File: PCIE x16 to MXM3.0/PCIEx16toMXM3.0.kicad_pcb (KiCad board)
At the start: 4 copper layers, 167.6 x 106.5 mm, 16 parts, among them J1 Bus_PCI_Express_x16, J2 MXM3.0, J4 2040210-1_NonStock, J5 74320-9010, U1 AMS1117-5.0

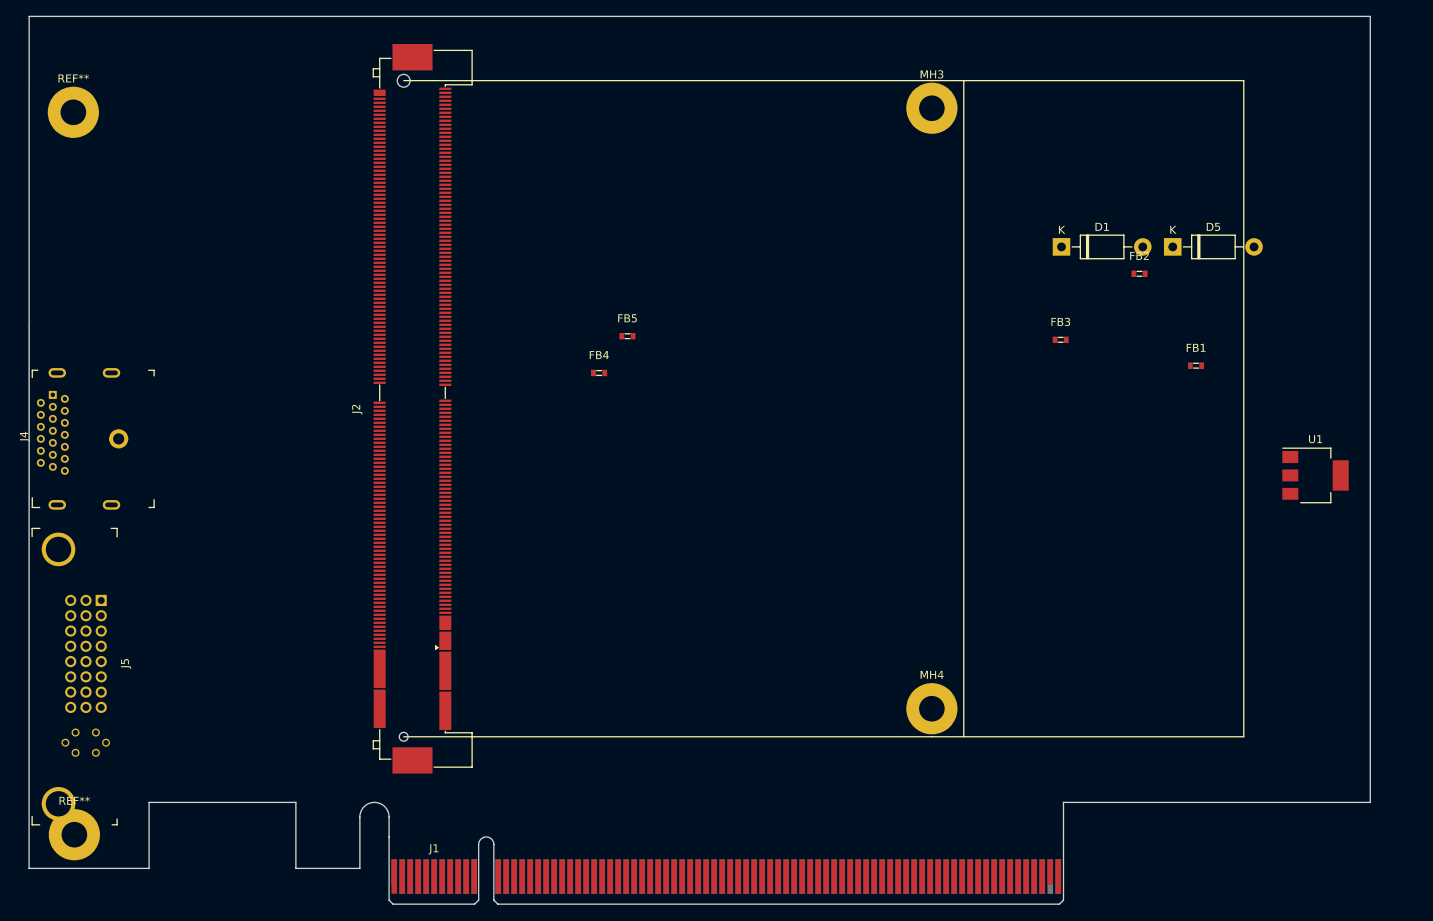
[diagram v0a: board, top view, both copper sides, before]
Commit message: Added x16 prototype
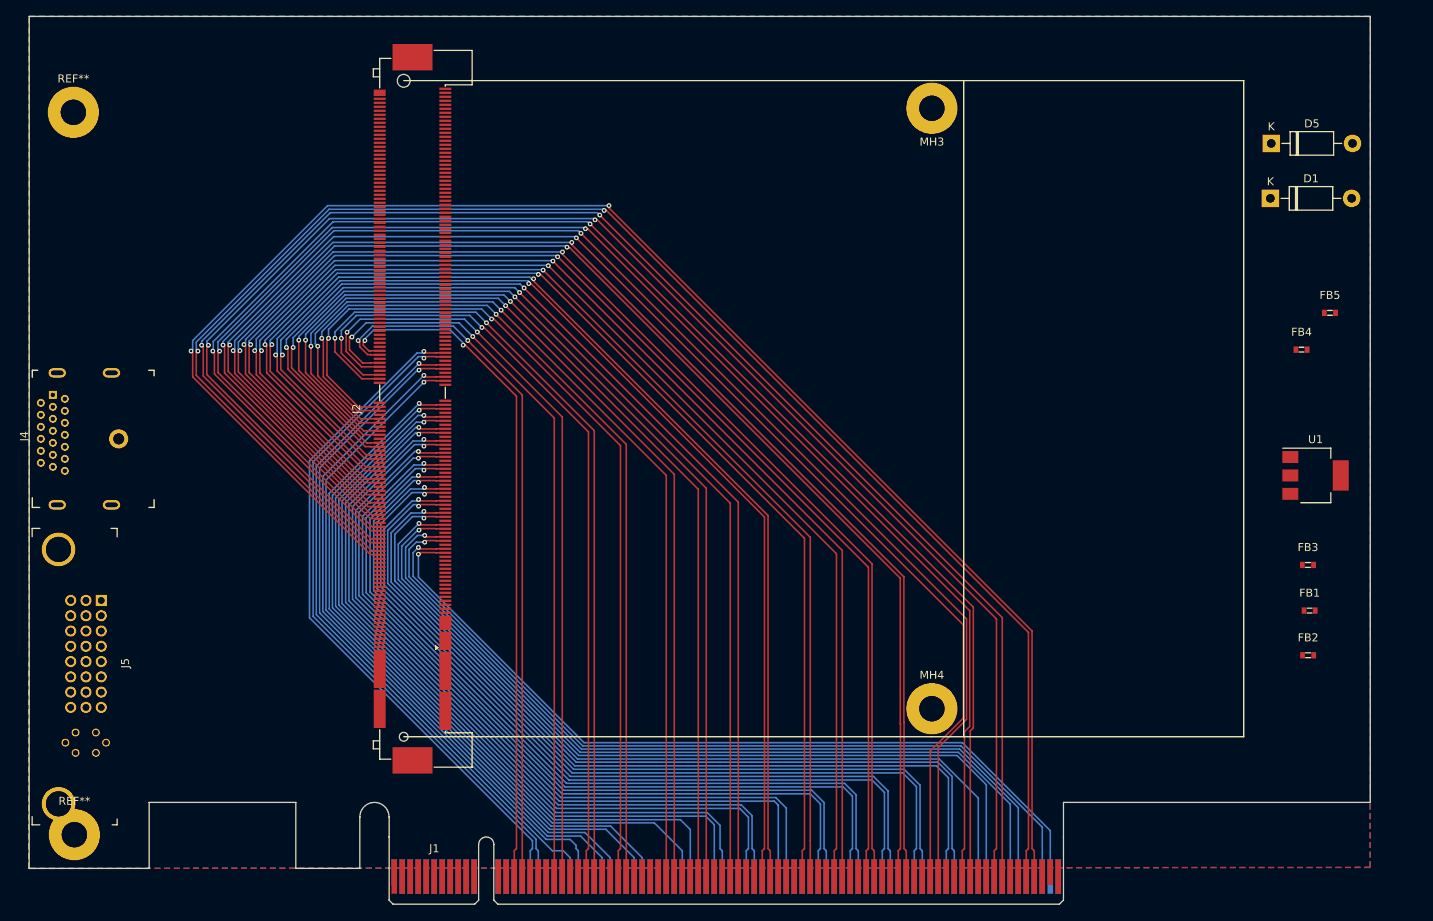
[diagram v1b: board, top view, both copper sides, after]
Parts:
- moved FB4 87.9 mm to (228.6, 78.3)
- moved FB5 87.9 mm to (232.1, 73.7)
- moved FB2 52.1 mm to (229.4, 116.5)
- moved FB3 41.8 mm to (229.4, 105.2)
- moved FB1 33.7 mm to (229.6, 110.9)
- moved D1 26.8 mm to (224.7, 59.4)
- moved D5 17.9 mm to (224.8, 52.5)
- turned MH3 to 180 degrees
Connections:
- MH3 pad 1: (no net) -> GND
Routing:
- net /PET15_N: track 0.00 -> 202.2 mm, vias 0 -> 2
- net /PET15_P: track 0.00 -> 199.8 mm, vias 0 -> 2
- net /PET14_N: track 0.00 -> 195.2 mm, vias 0 -> 2
- net /PET14_P: track 0.00 -> 192.6 mm, vias 0 -> 2
- net /PET13_N: track 0.00 -> 187.9 mm, vias 0 -> 2
- net /PET13_P: track 0.00 -> 185.6 mm, vias 0 -> 2
- net /PET12_N: track 0.00 -> 183.4 mm, vias 0 -> 2
- net /PET12_P: track 0.00 -> 180.8 mm, vias 0 -> 2
- net /PET11_N: track 0.00 -> 173.1 mm, vias 0 -> 2
- net /PET11_P: track 0.00 -> 170.7 mm, vias 0 -> 2
- net /PET10_N: track 0.00 -> 165.9 mm, vias 0 -> 2
- net /PET10_P: track 0.00 -> 163.3 mm, vias 0 -> 2
- net /PET9_N: track 0.00 -> 158.7 mm, vias 0 -> 2
- net /PET9_P: track 0.00 -> 156.1 mm, vias 0 -> 2
- net /PET8_N: track 0.00 -> 151.4 mm, vias 0 -> 2
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- added copper zone on B.Cu, net GND
- added copper zone on F.Cu, net GND

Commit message: Started work on x16 adapter
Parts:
- removed J5: 74320-9010, digikey-footprints:DVI_Female_74320-9010
- added D1: PMEG4010ET, Diode_SMD:D_SOT-23_ANK, F.Cu at (220.9, 63.0)
- added D5: PMEG4010ET, Diode_SMD:D_SOT-23_ANK, F.Cu at (225.4, 63.0)
- added D7: PMEG4010ET, Diode_SMD:D_SOT-23_ANK, F.Cu at (229.8, 63.0)
- added J3: 208658-1081, 2086581081, F.Cu at (76.0, 69.6)
- added Q1: BC848, Package_TO_SOT_SMD:SOT-23, F.Cu at (234.3, 63.0)
- J4: value 2040210-1_NonStock -> 45558-0003; footprint digikey-footprints:DisplayPort_2040210-1 -> 455580003
- moved J4 149.2 mm to (225.0, 51.7), turned to 0 degrees
- moved D5 70.4 mm to (224.2, 123.0)
- moved D1 70.4 mm to (224.1, 129.8)
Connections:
- net Net-(J1-PadA13) renamed /REFCLK_P
- net Net-(J1-PadA14) renamed /REFCLK_N
- net Net-(J1-PadB5) renamed /SMCLK
- net Net-(J1-PadB6) renamed /SMDAT
- net Net-(J2-Pad2) renamed /PRSNT_R#
- net Net-(J2-Pad21) renamed /VGA_DISABLE#
- net Net-(J2-Pad230) renamed /DP_D_AUX#
- net Net-(J2-Pad232) renamed /DP_D_AUX
- net Net-(J2-Pad236) renamed /DP_D_HPD
- net Net-(J2-Pad24) renamed TH_PWM
- net Net-(J2-Pad8) renamed Enable
- net PERST renamed /PERST
- net WAKE renamed /WAKE
- J1 pad B10: Net-(J1-PadB10) -> +3.3VA
- J1 pad B17: Net-(J1-PadB17) -> Net-(J1-PadA1)
- J2 pad 154: Net-(J1-PadB12) -> Net-(J2-Pad154)
- J2 pad 176: Net-(J2-Pad176) -> /CK_N
- J2 pad 178: Net-(J2-Pad178) -> /CK_P
- J2 pad 188: Net-(J2-Pad188) -> /D2_N
- J2 pad 190: Net-(J2-Pad190) -> /D2_P
- J2 pad 194: Net-(J2-Pad194) -> /D1_N
- J2 pad 196: Net-(J2-Pad196) -> /D1_P
- J2 pad 20: Net-(J2-Pad20) -> /TH_OVERT#
- J2 pad 200: Net-(J2-Pad200) -> /D0_N
- J2 pad 202: Net-(J2-Pad202) -> /D0_P
- J2 pad 206: Net-(J2-Pad206) -> /DP_D_L3#
- J2 pad 208: Net-(J2-Pad208) -> /DP_D_L3
- J2 pad 212: Net-(J2-Pad212) -> /DP_D_L3#
- J2 pad 214: Net-(J2-Pad214) -> /DP_D_L3
- J2 pad 218: Net-(J2-Pad218) -> /DP_D_L3#
- J2 pad 220: Net-(J2-Pad220) -> /DP_D_L3
- J2 pad 224: Net-(J2-Pad224) -> /DP_D_L3#
- J2 pad 226: Net-(J2-Pad226) -> /DP_D_L3
- J2 pad 276: Net-(J2-Pad276) -> /DP_A_HPD
- J2 pad 31: Net-(J2-Pad31) -> /TMDS_HPD
- J2 pad 33: Net-(J2-Pad33) -> /TMDS_SDA
- J2 pad 35: Net-(J2-Pad35) -> /TMDS_SCL
- J2 pad MP: (no net) -> GND
- J4 pad 1: Net-(C12-Pad2) -> +12V
- J4 pad 2: GND -> +12V
- J4 pad 3: Net-(C13-Pad2) -> +12V
- J4 pad 4: Net-(C10-Pad2) -> GND
- J4 pad 6: Net-(C11-Pad2) -> GND
- MH4 pad 1: (no net) -> GND
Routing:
- net /REFCLK_P: track 0.00 -> 87.3 mm, vias 0 -> 1
- net /REFCLK_N: track 0.00 -> 86.4 mm, vias 0 -> 1
- net /PERST: track 0.00 -> 82.9 mm, vias 0 -> 1
- net /SMDAT: track 0.00 -> 45.6 mm
- net /SMCLK: track 0.00 -> 45.4 mm
- net /WAKE: track 0.00 -> 41.4 mm
- net +12V: track 0.00 -> 28.8 mm, vias 0 -> 9
- net GND: track 0.00 -> 8.30 mm
- net /PER1_P: track 86.8 -> 87.5 mm

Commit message: Made progress on PCIE x16 adapter
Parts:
- J3: footprint 2086581081 -> SamacSys_Parts:2086581081
- moved J4 11.7 mm to (228.0, 40.4), turned to 270 degrees
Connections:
- REF** pad 1: (no net) -> GND (x2)
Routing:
- net +12V: track 28.8 -> 228.9 mm, vias 9 -> 13
- net +3V3: track 0.00 -> 136.3 mm, vias 0 -> 4
- net GND: track 8.30 -> 41.1 mm, vias 0 -> 8
- net /SMCLK: track 45.4 -> 46.0 mm
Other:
- board size 167.6 x 106.5 mm -> 173.5 x 106.5 mm

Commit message: Updated parts
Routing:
- net /PER3_P: track 87.1 -> 89.3 mm
- net /PER4_P: track 90.8 -> 92.8 mm
- net /PER3_N: track 86.7 -> 88.5 mm
- net /PER2_P: track 87.6 -> 89.0 mm
- net /PER13_P: track 105.1 -> 106.3 mm
- net /PER2_N: track 87.0 -> 88.1 mm
- net /PET15_P: track 199.8 -> 199.2 mm
- net /PET14_P: track 192.6 -> 192.0 mm
- net GND: vias 8 -> 42
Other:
- net class PER* added: clearance 0.127, trace_width 0.25, via_dia 0.6, via_drill 0.3
- net class PET* added: clearance 0.127, trace_width 0.25, via_dia 0.6, via_drill 0.3
- rule trace_min: 0.2 -> 0.127

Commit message: Made some changes
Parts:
- moved D1 5.52 mm to (226.4, 63.6)
- moved D5 5.52 mm to (230.9, 63.6)
- moved D7 5.52 mm to (235.3, 63.6)
- moved Q1 5.52 mm to (239.8, 63.6)
- moved U1 3.49 mm to (231.6, 90.8)
- moved D1 3.03 mm to (226.7, 128.2)
- moved D5 3.03 mm to (226.8, 121.3)
- moved FB1 3.03 mm to (232.1, 109.2)
- moved FB2 3.03 mm to (231.9, 114.8)
- moved FB3 3.03 mm to (231.9, 103.5)
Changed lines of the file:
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@@
   )
   (module Diode_THT:D_DO-41_SOD81_P10.16mm_Horizontal (layer F.Cu)
-    (at 224.124201 129.829401)
+    (at 226.651501 128.153001)
     (descr "Diode, DO-41_SOD81 series, Axial, Horizontal, pin pitch=10.16mm, , length*diameter=5.2*2.7mm^2, , http://www.diodes.com/_files/packages/DO-41%20(Plastic).pdf")
     (tags "Diode DO-41_SOD81 series Axial Horizontal pin pitch 10.16mm  length 5.2mm diameter 2.7mm")
@@
   )
   (module Diode_THT:D_DO-41_SOD81_P10.16mm_Horizontal (layer F.Cu)
-    (at 224.2312 122.9614)
+    (at 226.7585 121.285)
     (descr "Diode, DO-41_SOD81 series, Axial, Horizontal, pin pitch=10.16mm, , length*diameter=5.2*2.7mm^2, , http://www.diodes.com/_files/packages/DO-41%20(Plastic).pdf")
     (tags "Diode DO-41_SOD81 series Axial Horizontal pin pitch 10.16mm  length 5.2mm diameter 2.7mm")
@@
   )
   (module digikey-footprints:0603 (layer F.Cu)
-    (at 229.5906 110.9218)
+    (at 232.1179 109.2454)
     (attr smd)
     (fp_text reference FB1 (at 0 -2.2) (layer F.SilkS)
@@
   )
   (module digikey-footprints:0603 (layer F.Cu)
-    (at 229.4016 116.5098)
+    (at 231.9289 114.8334)
     (attr smd)
     (fp_text reference FB2 (at 0 -2.2) (layer F.SilkS)
@@
   )
   (module digikey-footprints:0603 (layer F.Cu)
-    (at 229.383601 105.219001)
+    (at 231.910901 103.542601)
     (attr smd)
     (fp_text reference FB3 (at 0 -2.2) (layer F.SilkS)
@@
   )
   (module Package_TO_SOT_SMD:SOT-223-3_TabPin2 (layer F.Cu)
-    (at 230.3272 94.0308)
+    (at 231.5972 90.7796)
     (descr "module CMS SOT223 4 pins")
     (tags "CMS SOT")
@@
   )
   (module Diode_SMD:D_SOT-23_ANK (layer F.Cu)
-    (at 220.925001 62.999601)
+    (at 226.411401 63.571101)
     (descr "SOT-23, Single Diode")
     (tags SOT-23)
@@
   )
   (module Diode_SMD:D_SOT-23_ANK (layer F.Cu)
-    (at 225.375001 62.999601)
+    (at 230.861401 63.571101)
     (descr "SOT-23, Single Diode")
     (tags SOT-23)
@@
   )
   (module Diode_SMD:D_SOT-23_ANK (layer F.Cu)
-    (at 229.825001 62.999601)
+    (at 235.311401 63.571101)
     (descr "SOT-23, Single Diode")
     (tags SOT-23)
@@
   )
   (module Package_TO_SOT_SMD:SOT-23 (layer F.Cu)
-    (at 234.275001 62.999601)
+    (at 239.761401 63.571101)
     (descr "SOT-23, Standard")
     (tags SOT-23)
